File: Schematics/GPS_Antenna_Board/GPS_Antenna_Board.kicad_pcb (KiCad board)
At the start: 2 copper layers, 50 x 65 mm, 28 parts, among them J2 SATA Conn. (Male), U1 SAM-M10Q, U2 LM66100DCKR

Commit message: Final Revisions
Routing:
- net GND: track 12.3 -> 11.5 mm
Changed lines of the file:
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@@
     (effects (font (size 1.2 1.2) (thickness 0.2) bold) (justify bottom))
   )
-  (segment (start 136.8 135.15) (end 136.8 134.4) (width 0.3) (layer "F.Cu") (net 1))
   (segment (start 136.85 136.4755) (end 136.85 135.53995) (width 0.5) (layer "F.Cu") (net 1))
   (segment (start 136.8745 136.5) (end 136.85 136.4755) (width 0.5) (layer "F.Cu") (net 1))
@@
   (segment (start 153.3 101.389339) (end 153.3 123.589472) (width 0.3) (layer "B.Cu") (net 6))
   (segment (start 147.010661 95.1) (end 153.3 101.389339) (width 0.3) (layer "B.Cu") (net 6))
-  (segment (start 151.3755 134.925) (end 150.341585 134.925) (width 0.3) (layer "F.Cu") (net 7))
+  (segment (start 150.341585 134.925) (end 158.5 134.925) (width 0.3) (layer "F.Cu") (net 7))
   (segment (start 158.5 134.925) (end 159.947182 134.925) (width 0.3) (layer "F.Cu") (net 7))
   (segment (start 159.947182 134.925) (end 161.397182 136.375) (width 0.3) (layer "F.Cu") (net 7))
@@
   (segment (start 147.7 94.4995) (end 147.7 92) (width 0.3) (layer "F.Cu") (net 7))
   (segment (start 148.2 130.0505) (end 148.199999 128.095301) (width 0.3) (layer "F.Cu") (net 7))
-  (segment (start 151.3755 134.925) (end 158.5 134.925) (width 0.3) (layer "F.Cu") (net 7))
   (segment (start 150.341585 134.925) (end 148.2 132.783415) (width 0.3) (layer "F.Cu") (net 7))
   (segment (start 148.199999 125.6505) (end 148.199999 128.095301) (width 0.3) (layer "F.Cu") (net 7))
@@
   (segment (start 146.929999 125.607571) (end 146.929999 128.095301) (width 0.3) (layer "F.Cu") (net 8))
   (segment (start 147.63707 124.9005) (end 146.929999 125.607571) (width 0.3) (layer "F.Cu") (net 8))
-  (segment (start 146.9 128.1253) (end 146.929999 128.095301) (width 0.5) (layer "F.Cu") (net 8))
   (segment (start 148.56574 124.95558) (end 148.51066 124.9005) (width 0.3) (layer "F.Cu") (net 8))
   (segment (start 149.6 106.4) (end 149.6 104.2) (width 0.3) (layer "F.Cu") (net 8))
@@
   (segment (start 164.55558 124.95558) (end 148.56574 124.95558) (width 0.3) (layer "F.Cu") (net 8))
   (segment (start 148.51066 124.9005) (end 147.63707 124.9005) (width 0.3) (layer "F.Cu") (net 8))
-  (segment (start 146.929999 125.607571) (end 146.929999 125.409339) (width 0.3) (layer "F.Cu") (net 8))
   (via (at 149.6 104.2) (size 0.8) (drill 0.4) (layers "F.Cu" "B.Cu") (net 8))
   (via (at 146.929999 125.607571) (size 0.8) (drill 0.4) (layers "F.Cu" "B.Cu") (net 8))
@@
   (segment (start 148.51066 126.4005) (end 150.219478 124.691682) (width 0.3) (layer "B.Cu") (net 9))
   (segment (start 146.176017 126.263709) (end 146.312808 126.4005) (width 0.3) (layer "B.Cu") (net 9))
-  (segment (start 144.4 128.105302) (end 144.389999 128.095301) (width 0.5) (layer "F.Cu") (net 10))
   (segment (start 144.389999 126.970662) (end 144.389999 128.095301) (width 0.3) (layer "F.Cu") (net 10))
   (segment (start 145.8 106.4) (end 145.8 104.2) (width 0.3) (layer "F.Cu") (net 10))
@@
   (segment (start 144.389999 130.040499) (end 144.4 130.0505) (width 0.3) (layer "F.Cu") (net 10))
   (segment (start 144.389999 128.095301) (end 144.389999 130.040499) (width 0.3) (layer "F.Cu") (net 10))
-  (segment (start 144.4 132.5245) (end 144.4245 132.5245) (width 0.5) (layer "F.Cu") (net 10))
   (segment (start 165.6 137.6) (end 169.275 137.6) (width 0.3) (layer "F.Cu") (net 10))
   (segment (start 144.4 132.5245) (end 149.9255 138.05) (width 0.3) (layer "F.Cu") (net 10))
@@
   (segment (start 169.6 133.9) (end 169.6 135.625) (width 0.5) (layer "F.Cu") (net 11))
   (segment (start 161.9 133.9) (end 161.9 135.625) (width 0.5) (layer "F.Cu") (net 12))
-  (segment (start 136.25 128.575) (end 136.3 128.525) (width 0.5) (layer "F.Cu") (net 13))
   (segment (start 137.786396 131.65) (end 136.463604 131.65) (width 0.5) (layer "F.Cu") (net 13))
   (segment (start 137.786396 131.65) (end 136.3 130.163604) (width 0.5) (layer "F.Cu") (net 13))

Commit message: Version bump
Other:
- board text added: "Gouda Rev 1.1 QRET May 2024 Tristan Alderson Kennan Bays"
- board text removed: "Gouda Rev 1.0 QRET Mar 2024 Tristan Alderson Kennan Bays"
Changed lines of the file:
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@@
   (gr_arc (start 171 74.2) (mid 172.202082 74.697918) (end 172.7 75.9)
     (stroke (width 0.1) (type default)) (layer "Edge.Cuts"))
-  (gr_text "Gouda Rev 1.0\nQRET Mar 2024\n\nTristan Alderson\nKennan Bays" (at 147.7 85.35) (layer "B.SilkS")
+  (gr_text "Gouda Rev 1.1\nQRET May 2024\n\nTristan Alderson\nKennan Bays" (at 147.7 85.35) (layer "B.SilkS")
     (effects (font (size 1.5 1.5) (thickness 0.25)) (justify top mirror))
   )

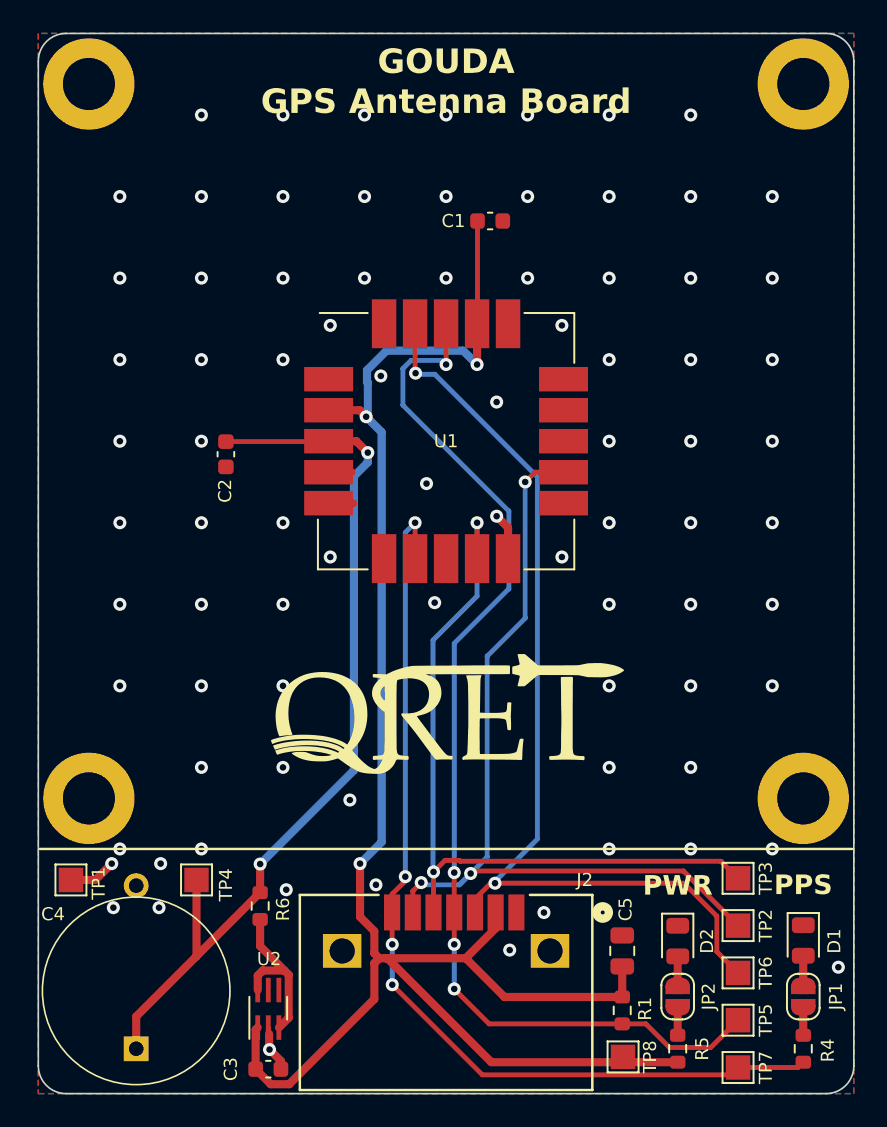
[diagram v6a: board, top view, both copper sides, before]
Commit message: Fixed SATA pinout + Dimmed power LED
Most SATA cables short pins 1,4,7 together as GND. For Rev 1.0, this meant the PPS, RESET, and GND pins were all tied together, effectively bricking the GPS.

This has been revised by disconnecting pins 4 & 7, discarding the PPS signal entirely and then sharing pin 3 for EITHER the reset signal or external interrupt signal. Updated board routing as needed.

Also quickly tweaked the power LED resistor so the LED is dimmer. (1.8k to 3.3k)
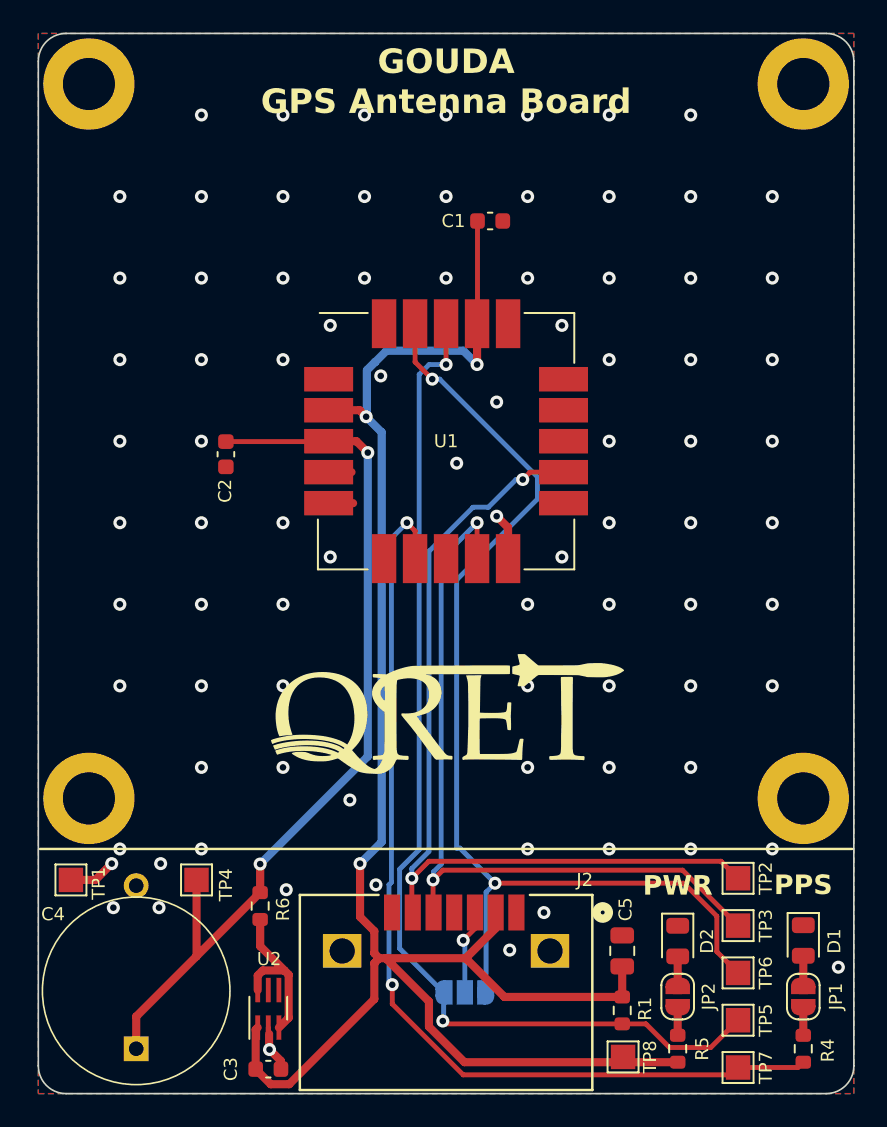
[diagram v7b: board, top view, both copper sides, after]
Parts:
- added JP3: P3 FUNC, Jumper:SolderJumper-3_P1.3mm_Open_RoundedPad1.0x1.5mm, B.Cu at (148.8, 133.0)
- moved TP2 2.90 mm to (165.6, 126.0)
- moved TP3 2.90 mm to (165.6, 128.9)
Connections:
- J2 pad 3: GPS_EXTINT -> Net-(JP3-C)
- J2 pad 4: GPS_RST -> unconnected-(J2-Pad4)
- J2 pad 7: GPS_PPS -> unconnected-(J2-Pad7)
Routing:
- net GPS_EXTINT: track 60.0 -> 66.2 mm
- net Net-(JP3-C): track 0.00 -> 5.24 mm, vias 0 -> 1
- net GPS_RST: track 67.2 -> 65.1 mm, vias 4 -> 2
- net SCL: track 52.2 -> 53.7 mm, vias 3 -> 2
- net SDA: track 46.6 -> 47.6 mm
- net +3.3V: track 113.3 -> 114.2 mm
- net GPS_PPS: track 58.9 -> 59.8 mm, vias 4 -> 2
- net GND: vias 83 -> 86
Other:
- board text added: "EXTINT"
- board text added: "P3 USE"
- board text added: "RESET"

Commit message: Fixed supercap charger RCB
Previous use of LM66100 ideal diode didn't work as, when power was lost, the ideal diode would stop functioning properly and would still let power through. Have swapped to a simple 1N5819 Schottky diode.

Also broke out the TX/RX pins of the GPS for easier external programming, if needed.
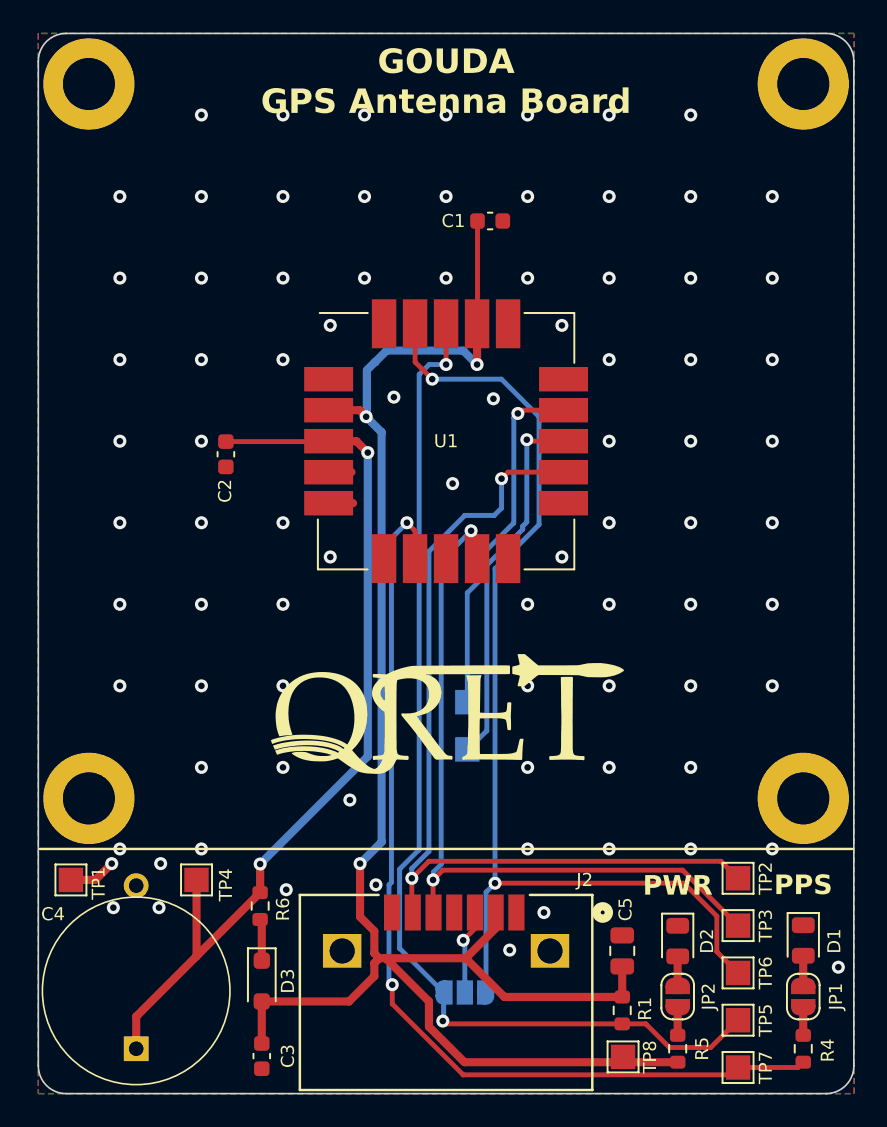
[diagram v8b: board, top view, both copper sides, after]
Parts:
- removed U2: LM66100DCKR, LMR66100:SC-70-6_Handsoldering
- added D3: 1N5819WS, Diode_SMD:D_SOD-323_HandSoldering, F.Cu at (136.4, 132.3)
- added TP10: TX, TestPoint:TestPoint_Pad_1.5x1.5mm, B.Cu at (149.0, 118.1)
- added TP9: RX, TestPoint:TestPoint_Pad_1.5x1.5mm, B.Cu at (149.0, 115.2)
- R5: value 1.8k -> 3.3k
- moved C3 0.89 mm to (136.4, 136.9), turned to -90 degrees
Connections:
- U1 pad 13: unconnected-(U1-TXD-Pad13) -> Net-(U1-TXD)
- U1 pad 14: unconnected-(U1-RXD-Pad14) -> Net-(U1-RXD)
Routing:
- net Net-(U1-TXD): track 0.00 -> 22.8 mm, vias 0 -> 1
- net Net-(U1-RXD): track 0.00 -> 21.9 mm, vias 0 -> 1
- net Net-(D3-K): track 10.3 -> 2.57 mm
- net GND: track 11.5 -> 5.77 mm, vias 86 -> 84
- net +3.3V: track 114.2 -> 110.5 mm
- net SCL: track 53.7 -> 54.8 mm
- net SDA: track 47.6 -> 46.6 mm
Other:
- board text added: "RX"
- board text added: "TX"
